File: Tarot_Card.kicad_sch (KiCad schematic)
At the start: 25 parts, among them U2 ESP32-PICO-D4

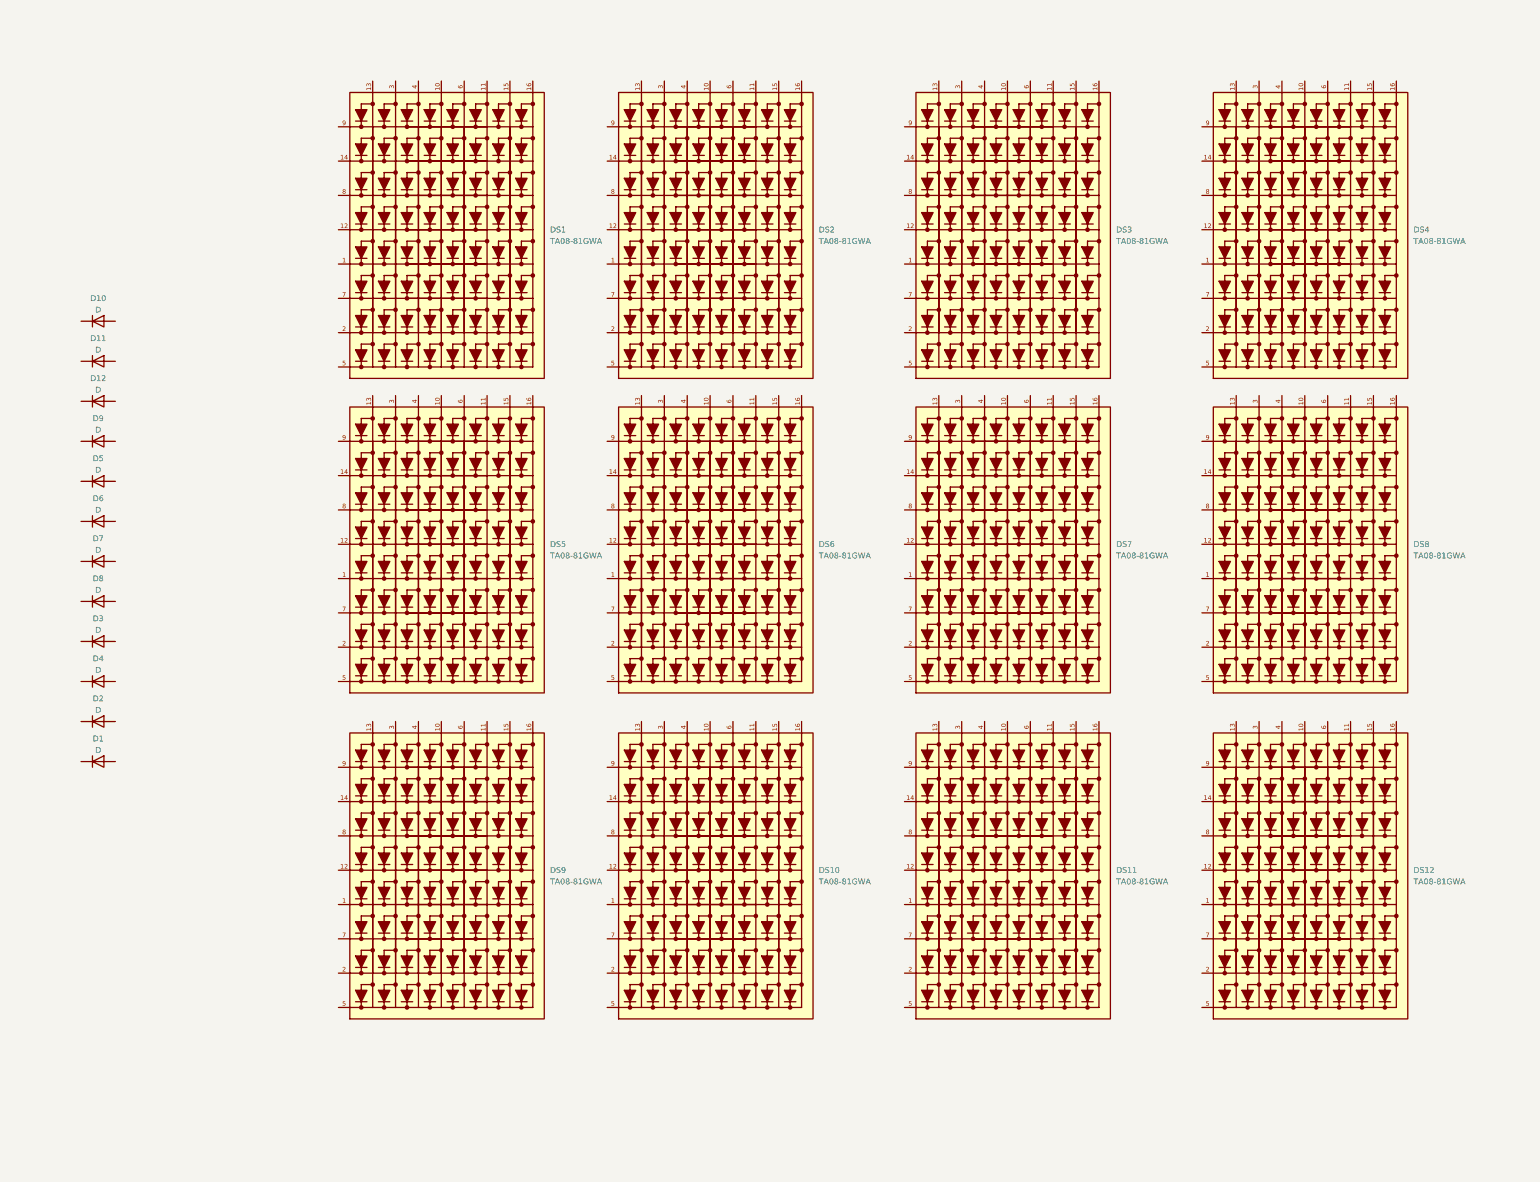
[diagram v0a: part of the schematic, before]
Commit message: Remove obsolete lock files and backups; update project configuration for ngspice integration
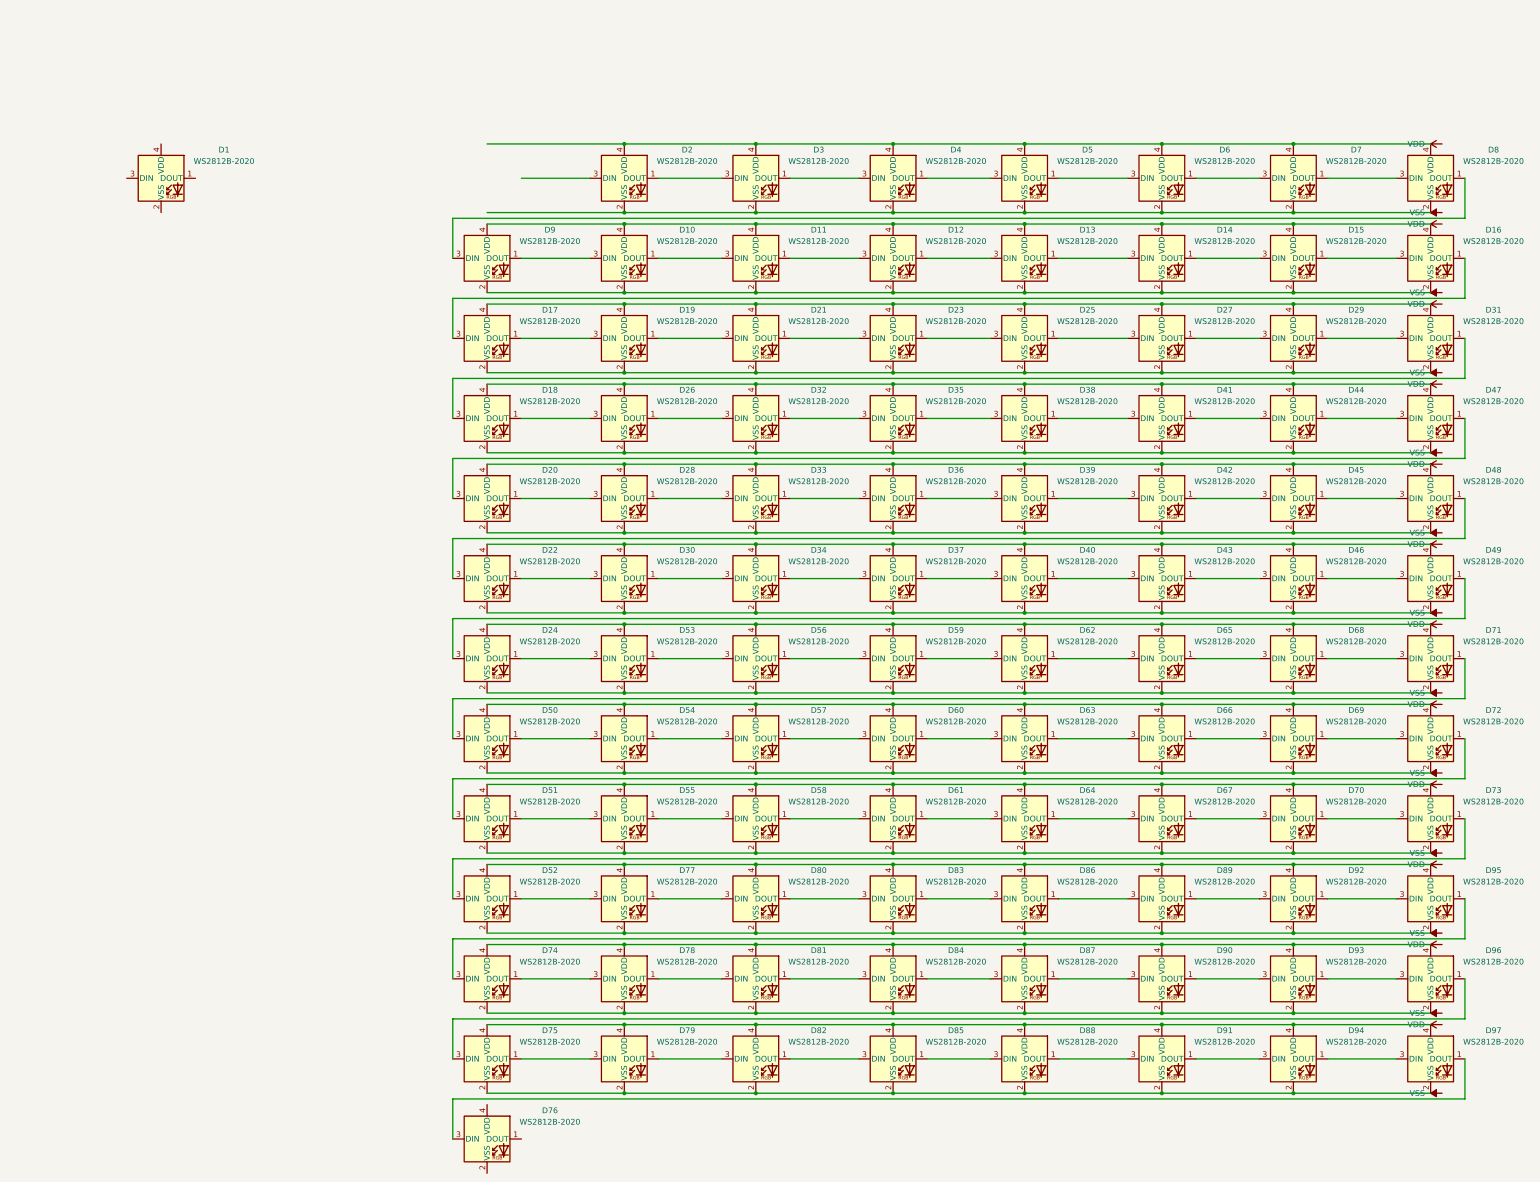
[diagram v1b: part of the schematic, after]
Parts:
- removed D1, D10, D11, D12, D2, D3, D4, D5, D6, D7, D8, D9: D, symbol Device:D
- removed DS1, DS10, DS11, DS12, DS2, DS3, DS4, DS5, DS6, DS7, DS8, DS9: TA08-81GWA, Parts:DISPLAY_TA08-81GWA, symbol TA08-81GWA:TA08-81GWA
- added D1, D10, D11, D12, D13, D14, D15, D16, D17, D18, D19, D2, D20, D21, D22, D23, D24, D25, D26, D27, D28, D29, D3, D30, D31, D32, D33, D34, D35, D36, D37, D38, D39, D4, D40, D41, D42, D43, D44, D45, D46, D47, D48, D49, D5, D50, D51, D52, D53, D54, D55, D56, D57, D58, D59, D6, D60, D61, D62, D63, D64, D65, D66, D67, D68, D69, D7, D70, D71, D72, D73, D74, D75, D76, D77, D78, D79, D8, D80, D81, D82, D83, D84, D85, D86, D87, D88, D89, D9, D90, D91, D92, D93, D94, D95, D96, D97: WS2812B-2020, LED_SMD:LED_WS2812B-2020_PLCC4_2.0x2.0mm, symbol LED:WS2812B-2020
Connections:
- new net: D91.1 (DOUT), D94.3 (DIN)
- new net: D75.2 (VSS), D79.2 (VSS), D82.2 (VSS), D85.2 (VSS), D88.2 (VSS), D91.2 (VSS), D94.2 (VSS), D97.2 (VSS)
- new net: D88.1 (DOUT), D91.3 (DIN)
- new net: D75.4 (VDD), D79.4 (VDD), D82.4 (VDD), D85.4 (VDD), D88.4 (VDD), D91.4 (VDD), D94.4 (VDD), D97.4 (VDD)
- new net: D85.1 (DOUT), D88.3 (DIN)
- new net: D82.1 (DOUT), D85.3 (DIN)
- new net: D90.1 (DOUT), D93.3 (DIN)
- new net: D74.2 (VSS), D78.2 (VSS), D81.2 (VSS), D84.2 (VSS), D87.2 (VSS), D90.2 (VSS), D93.2 (VSS), D96.2 (VSS)
- new net: D87.1 (DOUT), D90.3 (DIN)
- new net: D74.4 (VDD), D78.4 (VDD), D81.4 (VDD), D84.4 (VDD), D87.4 (VDD), D90.4 (VDD), D93.4 (VDD), D96.4 (VDD)
- new net: D75.3 (DIN), D96.1 (DOUT)
- new net: D93.1 (DOUT), D96.3 (DIN)
- new net: D43.1 (DOUT), D46.3 (DIN)
- new net: D22.2 (VSS), D30.2 (VSS), D34.2 (VSS), D37.2 (VSS), D40.2 (VSS), D43.2 (VSS), D46.2 (VSS), D49.2 (VSS)
- new net: D40.1 (DOUT), D43.3 (DIN)
- new net: D22.4 (VDD), D30.4 (VDD), D34.4 (VDD), D37.4 (VDD), D40.4 (VDD), D43.4 (VDD), D46.4 (VDD), D49.4 (VDD)
- new net: D54.1 (DOUT), D57.3 (DIN)
- new net: D50.2 (VSS), D54.2 (VSS), D57.2 (VSS), D60.2 (VSS), D63.2 (VSS), D66.2 (VSS), D69.2 (VSS), D72.2 (VSS)
- new net: D50.1 (DOUT), D54.3 (DIN)
- new net: D50.4 (VDD), D54.4 (VDD), D57.4 (VDD), D60.4 (VDD), D63.4 (VDD), D66.4 (VDD), D69.4 (VDD), D72.4 (VDD)
- new net: D70.1 (DOUT), D73.3 (DIN)
- new net: D51.2 (VSS), D55.2 (VSS), D58.2 (VSS), D61.2 (VSS), D64.2 (VSS), D67.2 (VSS), D70.2 (VSS), D73.2 (VSS)
- new net: D67.1 (DOUT), D70.3 (DIN)
- new net: D51.4 (VDD), D55.4 (VDD), D58.4 (VDD), D61.4 (VDD), D64.4 (VDD), D67.4 (VDD), D70.4 (VDD), D73.4 (VDD)
- new net: D6.1 (DOUT), D7.3 (DIN)
- new net: D2.2 (VSS), D3.2 (VSS), D4.2 (VSS), D5.2 (VSS), D6.2 (VSS), D7.2 (VSS), D8.2 (VSS)
- new net: D5.1 (DOUT), D6.3 (DIN)
- new net: D2.4 (VDD), D3.4 (VDD), D4.4 (VDD), D5.4 (VDD), D6.4 (VDD), D7.4 (VDD), D8.4 (VDD)
- new net: D3.1 (DOUT), D4.3 (DIN)
- new net: D2.1 (DOUT), D3.3 (DIN)
- new net: D27.1 (DOUT), D29.3 (DIN)
- new net: D17.2 (VSS), D19.2 (VSS), D21.2 (VSS), D23.2 (VSS), D25.2 (VSS), D27.2 (VSS), D29.2 (VSS), D31.2 (VSS)
- new net: D25.1 (DOUT), D27.3 (DIN)
- new net: D17.4 (VDD), D19.4 (VDD), D21.4 (VDD), D23.4 (VDD), D25.4 (VDD), D27.4 (VDD), D29.4 (VDD), D31.4 (VDD)
- new net: D26.1 (DOUT), D32.3 (DIN)
- new net: D18.2 (VSS), D26.2 (VSS), D32.2 (VSS), D35.2 (VSS), D38.2 (VSS), D41.2 (VSS), D44.2 (VSS), D47.2 (VSS)
- new net: D18.1 (DOUT), D26.3 (DIN)
- new net: D18.4 (VDD), D26.4 (VDD), D32.4 (VDD), D35.4 (VDD), D38.4 (VDD), D41.4 (VDD), D44.4 (VDD), D47.4 (VDD)
- new net: D10.1 (DOUT), D11.3 (DIN)
- new net: D10.2 (VSS), D11.2 (VSS), D12.2 (VSS), D13.2 (VSS), D14.2 (VSS), D15.2 (VSS), D16.2 (VSS), D9.2 (VSS)
- new net: D10.3 (DIN), D9.1 (DOUT)
- new net: D10.4 (VDD), D11.4 (VDD), D12.4 (VDD), D13.4 (VDD), D14.4 (VDD), D15.4 (VDD), D16.4 (VDD), D9.4 (VDD)
- new net: D53.1 (DOUT), D56.3 (DIN)
- new net: D24.2 (VSS), D53.2 (VSS), D56.2 (VSS), D59.2 (VSS), D62.2 (VSS), D65.2 (VSS), D68.2 (VSS), D71.2 (VSS)
- new net: D24.1 (DOUT), D53.3 (DIN)
- new net: D24.4 (VDD), D53.4 (VDD), D56.4 (VDD), D59.4 (VDD), D62.4 (VDD), D65.4 (VDD), D68.4 (VDD), D71.4 (VDD)
- new net: D22.1 (DOUT), D30.3 (DIN)
- new net: D22.3 (DIN), D48.1 (DOUT)
- new net: D17.1 (DOUT), D19.3 (DIN)
- new net: D16.1 (DOUT), D17.3 (DIN)
- new net: D52.1 (DOUT), D77.3 (DIN)
- new net: D52.2 (VSS), D77.2 (VSS), D80.2 (VSS), D83.2 (VSS), D86.2 (VSS), D89.2 (VSS), D92.2 (VSS), D95.2 (VSS)
- new net: D52.3 (DIN), D73.1 (DOUT)
- new net: D52.4 (VDD), D77.4 (VDD), D80.4 (VDD), D83.4 (VDD), D86.4 (VDD), D89.4 (VDD), D92.4 (VDD), D95.4 (VDD)
- new net: D57.1 (DOUT), D60.3 (DIN)
- new net: D68.1 (DOUT), D71.3 (DIN)
- new net: D65.1 (DOUT), D68.3 (DIN)
- new net: D63.1 (DOUT), D66.3 (DIN)
- new net: D60.1 (DOUT), D63.3 (DIN)
- new net: D74.3 (DIN), D95.1 (DOUT)
- new net: D92.1 (DOUT), D95.3 (DIN)
- new net: D76.3 (DIN), D97.1 (DOUT)
- new net: D35.1 (DOUT), D38.3 (DIN)
- new net: D32.1 (DOUT), D35.3 (DIN)
- new net: D80.1 (DOUT), D83.3 (DIN)
- new net: D77.1 (DOUT), D80.3 (DIN)
- new net: D83.1 (DOUT), D86.3 (DIN)
- new net: D23.1 (DOUT), D25.3 (DIN)
- new net: D11.1 (DOUT), D12.3 (DIN)
- new net: D56.1 (DOUT), D59.3 (DIN)
- new net: D28.1 (DOUT), D33.3 (DIN)
- new net: D20.2 (VSS), D28.2 (VSS), D33.2 (VSS), D36.2 (VSS), D39.2 (VSS), D42.2 (VSS), D45.2 (VSS), D48.2 (VSS)
- new net: D20.1 (DOUT), D28.3 (DIN)
- new net: D20.4 (VDD), D28.4 (VDD), D33.4 (VDD), D36.4 (VDD), D39.4 (VDD), D42.4 (VDD), D45.4 (VDD), D48.4 (VDD)
- new net: D41.1 (DOUT), D44.3 (DIN)
- new net: D38.1 (DOUT), D41.3 (DIN)
- new net: D75.1 (DOUT), D79.3 (DIN)
- new net: D46.1 (DOUT), D49.3 (DIN)
- new net: D18.3 (DIN), D31.1 (DOUT)
- new net: D89.1 (DOUT), D92.3 (DIN)
- new net: D20.3 (DIN), D47.1 (DOUT)
- new net: D45.1 (DOUT), D48.3 (DIN)
- new net: D42.1 (DOUT), D45.3 (DIN)
- new net: D37.1 (DOUT), D40.3 (DIN)
- new net: D78.1 (DOUT), D81.3 (DIN)
- new net: D74.1 (DOUT), D78.3 (DIN)
- new net: D30.1 (DOUT), D34.3 (DIN)
- new net: D62.1 (DOUT), D65.3 (DIN)
- new net: D81.1 (DOUT), D84.3 (DIN)
- new net: D8.1 (DOUT), D9.3 (DIN)
- new net: D4.1 (DOUT), D5.3 (DIN)
- new net: D86.1 (DOUT), D89.3 (DIN)
- new net: D64.1 (DOUT), D67.3 (DIN)
- new net: D61.1 (DOUT), D64.3 (DIN)
- new net: D58.1 (DOUT), D61.3 (DIN)
- new net: D55.1 (DOUT), D58.3 (DIN)
- new net: D7.1 (DOUT), D8.3 (DIN)
- new net: D94.1 (DOUT), D97.3 (DIN)
- new net: D79.1 (DOUT), D82.3 (DIN)
- new net: D12.1 (DOUT), D13.3 (DIN)
- new net: D21.1 (DOUT), D23.3 (DIN)
- new net: D19.1 (DOUT), D21.3 (DIN)
- new net: D24.3 (DIN), D49.1 (DOUT)
- new net: D51.1 (DOUT), D55.3 (DIN)
- new net: D51.3 (DIN), D72.1 (DOUT)
- new net: D69.1 (DOUT), D72.3 (DIN)
- new net: D50.3 (DIN), D71.1 (DOUT)
- new net: D66.1 (DOUT), D69.3 (DIN)
- new net: D13.1 (DOUT), D14.3 (DIN)
- new net: D29.1 (DOUT), D31.3 (DIN)
- new net: D39.1 (DOUT), D42.3 (DIN)
- new net: D84.1 (DOUT), D87.3 (DIN)
- new net: D34.1 (DOUT), D37.3 (DIN)
- new net: D36.1 (DOUT), D39.3 (DIN)
- new net: D33.1 (DOUT), D36.3 (DIN)
- new net: D44.1 (DOUT), D47.3 (DIN)
- new net: D59.1 (DOUT), D62.3 (DIN)
- new net: D15.1 (DOUT), D16.3 (DIN)
- new net: D14.1 (DOUT), D15.3 (DIN)

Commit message: Remove obsolete backup file; update active layer and BOM export filename in project files
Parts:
- removed U2: ESP32-PICO-D4, Package_DFN_QFN:QFN-48-1EP_7x7mm_P0.5mm_EP5.3x5.3mm, symbol MCU_Espressif:ESP32-PICO-D4
- added D103, D104, D109, D110, D115, D116, D121, D122, D127, D128, D133, D134, D139, D140, D98: WS2812B-2020, LED_SMD:LED_WS2812B-2020_PLCC4_2.0x2.0mm, symbol LED:WS2812B-2020
- added U1: ESP32-S3-MINI-1U, RF_Module:ESP32-S2-MINI-1U, symbol RF_Module:ESP32-S3-MINI-1U
- added U4: ESP32-WROOM-32, RF_Module:ESP32-S3-WROOM-1, symbol RF_Module:ESP32-WROOM-32
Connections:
- net VDD: now also D1.4 (VDD), D10.4 (VDD), D11.4 (VDD), D12.4 (VDD), D13.4 (VDD), D14.4 (VDD), D15.4 (VDD), D16.4 (VDD), D17.4 (VDD), D18.4 (VDD), D19.4 (VDD), D2.4 (VDD), D20.4 (VDD), D21.4 (VDD), D22.4 (VDD), D23.4 (VDD), D24.4 (VDD), D25.4 (VDD), D26.4 (VDD), D27.4 (VDD), D28.4 (VDD), D29.4 (VDD), D3.4 (VDD), D30.4 (VDD), D31.4 (VDD), D32.4 (VDD), D33.4 (VDD), D34.4 (VDD), D35.4 (VDD), D36.4 (VDD), D37.4 (VDD), D38.4 (VDD), D39.4 (VDD), D4.4 (VDD), D40.4 (VDD), D41.4 (VDD), D42.4 (VDD), D43.4 (VDD), D44.4 (VDD), D45.4 (VDD), D46.4 (VDD), D47.4 (VDD), D48.4 (VDD), D49.4 (VDD), D5.4 (VDD), D50.4 (VDD), D51.4 (VDD), D52.4 (VDD), D53.4 (VDD), D54.4 (VDD), D55.4 (VDD), D56.4 (VDD), D57.4 (VDD), D58.4 (VDD), D59.4 (VDD), D6.4 (VDD), D60.4 (VDD), D61.4 (VDD), D62.4 (VDD), D63.4 (VDD), D64.4 (VDD), D65.4 (VDD), D66.4 (VDD), D67.4 (VDD), D68.4 (VDD), D69.4 (VDD), D7.4 (VDD), D70.4 (VDD), D71.4 (VDD), D72.4 (VDD), D73.4 (VDD), D74.4 (VDD), D75.4 (VDD), D76.4 (VDD), D77.4 (VDD), D78.4 (VDD), D79.4 (VDD), D8.4 (VDD), D80.4 (VDD), D81.4 (VDD), D82.4 (VDD), D83.4 (VDD), D84.4 (VDD), D85.4 (VDD), D86.4 (VDD), D87.4 (VDD), D88.4 (VDD), D89.4 (VDD), D9.4 (VDD), D90.4 (VDD), D91.4 (VDD), D92.4 (VDD), D93.4 (VDD), D94.4 (VDD), D95.4 (VDD), D96.4 (VDD), D97.4 (VDD), D103.4 (VDD), D104.4 (VDD), D109.4 (VDD), D110.4 (VDD), D115.4 (VDD), D116.4 (VDD), D121.4 (VDD), D122.4 (VDD), D127.4 (VDD), D128.4 (VDD), D133.4 (VDD), D134.4 (VDD), D139.4 (VDD), D140.4 (VDD), D98.4 (VDD), U1.3 (3V3)
- net VSS: now also D1.2 (VSS), D10.2 (VSS), D11.2 (VSS), D12.2 (VSS), D13.2 (VSS), D14.2 (VSS), D15.2 (VSS), D16.2 (VSS), D17.2 (VSS), D18.2 (VSS), D19.2 (VSS), D2.2 (VSS), D20.2 (VSS), D21.2 (VSS), D22.2 (VSS), D23.2 (VSS), D24.2 (VSS), D25.2 (VSS), D26.2 (VSS), D27.2 (VSS), D28.2 (VSS), D29.2 (VSS), D3.2 (VSS), D30.2 (VSS), D31.2 (VSS), D32.2 (VSS), D33.2 (VSS), D34.2 (VSS), D35.2 (VSS), D36.2 (VSS), D37.2 (VSS), D38.2 (VSS), D39.2 (VSS), D4.2 (VSS), D40.2 (VSS), D41.2 (VSS), D42.2 (VSS), D43.2 (VSS), D44.2 (VSS), D45.2 (VSS), D46.2 (VSS), D47.2 (VSS), D48.2 (VSS), D49.2 (VSS), D5.2 (VSS), D50.2 (VSS), D51.2 (VSS), D52.2 (VSS), D53.2 (VSS), D54.2 (VSS), D55.2 (VSS), D56.2 (VSS), D57.2 (VSS), D58.2 (VSS), D59.2 (VSS), D6.2 (VSS), D60.2 (VSS), D61.2 (VSS), D62.2 (VSS), D63.2 (VSS), D64.2 (VSS), D65.2 (VSS), D66.2 (VSS), D67.2 (VSS), D68.2 (VSS), D69.2 (VSS), D7.2 (VSS), D70.2 (VSS), D71.2 (VSS), D72.2 (VSS), D73.2 (VSS), D74.2 (VSS), D75.2 (VSS), D76.2 (VSS), D77.2 (VSS), D78.2 (VSS), D79.2 (VSS), D8.1 (DOUT), D8.2 (VSS), D80.2 (VSS), D81.2 (VSS), D82.2 (VSS), D83.2 (VSS), D84.2 (VSS), D85.2 (VSS), D86.2 (VSS), D87.2 (VSS), D88.2 (VSS), D89.2 (VSS), D9.2 (VSS), D9.3 (DIN), D90.2 (VSS), D91.2 (VSS), D92.2 (VSS), D93.2 (VSS), D94.2 (VSS), D95.2 (VSS), D96.2 (VSS), D97.2 (VSS), D103.2 (VSS), D104.2 (VSS), D109.2 (VSS), D110.2 (VSS), D115.2 (VSS), D116.2 (VSS), D121.2 (VSS), D122.2 (VSS), D127.2 (VSS), D128.2 (VSS), D133.2 (VSS), D134.2 (VSS), D139.2 (VSS), D140.2 (VSS), D98.2 (VSS), U1.1 (GND), U1.2 (GND), U1.42 (GND), U1.43 (GND), U1.46 (GND), U1.47 (GND), U1.48 (GND), U1.49 (GND), U1.50 (GND), U1.51 (GND), U1.52 (GND), U1.53 (GND), U1.54 (GND), U1.55 (GND), U1.56 (GND), U1.57 (GND), U1.58 (GND), U1.59 (GND), U1.60 (GND), U1.61 (GND), U1.62 (GND), U1.63 (GND), U1.64 (GND), U1.65 (GND)
- net at D91.1 (DOUT): now also D50.3 (DIN); no longer D94.3 (DIN)
- net at D91.3 (DIN): now also D85.1 (DOUT); no longer D88.1 (DOUT)
- net at D88.3 (DIN): now also D82.1 (DOUT); no longer D85.1 (DOUT)
- net at D85.3 (DIN): now also D79.1 (DOUT); no longer D82.1 (DOUT)
- net at D90.1 (DOUT): now also D96.3 (DIN); no longer D93.3 (DIN)
- net at D90.3 (DIN): now also D84.1 (DOUT); no longer D87.1 (DOUT)
- net at D96.1 (DOUT): now also D97.3 (DIN); no longer D75.3 (DIN)
- net at D93.1 (DOUT): now also D52.3 (DIN); no longer D96.3 (DIN)
- net at D57.3 (DIN): now also D51.1 (DOUT); no longer D54.1 (DOUT)
- net at D50.1 (DOUT): now also D56.3 (DIN); no longer D54.3 (DIN)
- net at D70.1 (DOUT): now also D76.3 (DIN); no longer D73.3 (DIN)
- net at D70.3 (DIN): now also D64.1 (DOUT); no longer D67.1 (DOUT)
- net at D6.3 (DIN): no longer D5.1 (DOUT)
- net at D53.1 (DOUT): now also D59.3 (DIN); no longer D56.3 (DIN)
- net at D24.1 (DOUT): now also D55.3 (DIN); no longer D53.3 (DIN)
- net at D77.3 (DIN): now also D71.1 (DOUT); no longer D52.1 (DOUT)
- net at D73.1 (DOUT): now also D79.3 (DIN); no longer D52.3 (DIN)
- net at D57.1 (DOUT): now also D63.3 (DIN); no longer D60.3 (DIN)
- net at D71.3 (DIN): now also D65.1 (DOUT); no longer D68.1 (DOUT)
- net at D68.3 (DIN): now also D62.1 (DOUT); no longer D65.1 (DOUT)
- net at D66.3 (DIN): now also D60.1 (DOUT); no longer D63.1 (DOUT)
- net at D74.3 (DIN): now also D68.1 (DOUT); no longer D95.1 (DOUT)
- net at D92.1 (DOUT): now also D51.3 (DIN); no longer D95.3 (DIN)
- net at D76.1 (DOUT): now also D82.3 (DIN)
- net at D97.1 (DOUT): now also D103.3 (DIN); no longer D76.3 (DIN)
- net at D83.3 (DIN): now also D77.1 (DOUT); no longer D80.1 (DOUT)
- net at D80.3 (DIN): now also D74.1 (DOUT); no longer D77.1 (DOUT)
- net at D83.1 (DOUT): now also D89.3 (DIN); no longer D86.3 (DIN)
- net at D56.1 (DOUT): now also D62.3 (DIN); no longer D59.3 (DIN)
- net at D75.1 (DOUT): now also D81.3 (DIN); no longer D79.3 (DIN)
- net at D92.3 (DIN): now also D86.1 (DOUT); no longer D89.1 (DOUT)
- net at D78.1 (DOUT): now also D84.3 (DIN); no longer D81.3 (DIN)
- net at D78.3 (DIN): now also D72.1 (DOUT); no longer D74.1 (DOUT)
- net at D65.3 (DIN): now also D59.1 (DOUT); no longer D62.1 (DOUT)
- net at D81.1 (DOUT): now also D87.3 (DIN); no longer D84.3 (DIN)
- net at D67.3 (DIN): now also D61.1 (DOUT); no longer D64.1 (DOUT)
- net at D64.3 (DIN): now also D58.1 (DOUT); no longer D61.1 (DOUT)
- net at D61.3 (DIN): now also D55.1 (DOUT); no longer D58.1 (DOUT)
- net at D58.3 (DIN): now also D52.1 (DOUT); no longer D55.1 (DOUT)
- net at D94.1 (DOUT): now also D53.3 (DIN); no longer D97.3 (DIN)
- net at D2.3 (DIN): now also D1.1 (DOUT)
- net DIN: now reaches D24.3 (DIN), D49.1 (DOUT)
- net DIN: now also D1.3 (DIN), U1.30 (IO48)
- net at D72.3 (DIN): now also D66.1 (DOUT); no longer D69.1 (DOUT)
- net at D69.3 (DIN): now also D63.1 (DOUT); no longer D66.1 (DOUT)
- new net: D103.1 (DOUT), D109.3 (DIN)
- new net: D67.1 (DOUT), D73.3 (DIN)
- new net: D121.1 (DOUT), D127.3 (DIN)
- new net: D115.1 (DOUT), D121.3 (DIN)
- new net: D128.1 (DOUT), D134.3 (DIN)
- new net: D122.1 (DOUT), D128.3 (DIN)
- new net: D104.3 (DIN), D98.1 (DOUT)
- new net: D139.1 (DOUT), D98.3 (DIN)
- new net: D134.1 (DOUT), D140.3 (DIN)
- new net: D104.1 (DOUT), D110.3 (DIN)
- new net: D88.1 (DOUT), D94.3 (DIN)
- new net: D87.1 (DOUT), D93.3 (DIN)
- new net: U4.1 (GND), U4.15 (GND), U4.38 (GND), U4.39 (GND)
- new net: D109.1 (DOUT), D115.3 (DIN)
- new net: D116.1 (DOUT), D122.3 (DIN)
- new net: D69.1 (DOUT), D75.3 (DIN)
- new net: D54.1 (DOUT), D60.3 (DIN)
- new net: D80.1 (DOUT), D86.3 (DIN)
- new net: D54.3 (DIN), D95.1 (DOUT)
- new net: D89.1 (DOUT), D95.3 (DIN)
- new net: D133.1 (DOUT), D139.3 (DIN)
- new net: D127.1 (DOUT), D133.3 (DIN)
- new net: D110.1 (DOUT), D116.3 (DIN)
- new net DOUT: D5.1 (DOUT), U1.27 (IO47)
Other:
- moved on the sheet: D1, D10, D11, D12, D13, D14, D15, D16, D17, D18, D19, D2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
